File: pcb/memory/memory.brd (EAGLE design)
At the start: 50 x 80 mm, 9 parts, among them IC1 CY62256LL-PXC, IC2 CY62256LL-PXC, IC3 74HC04D

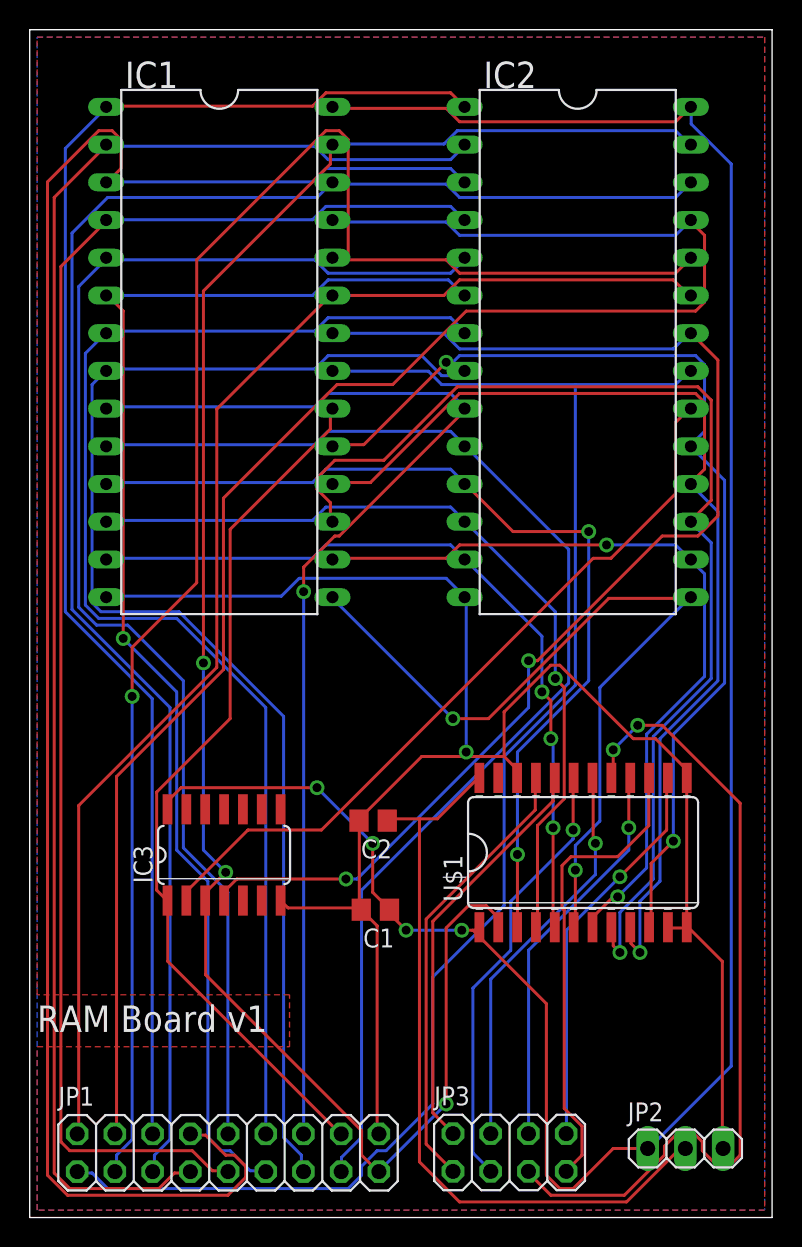
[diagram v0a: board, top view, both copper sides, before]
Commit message: Fixed pours and borders
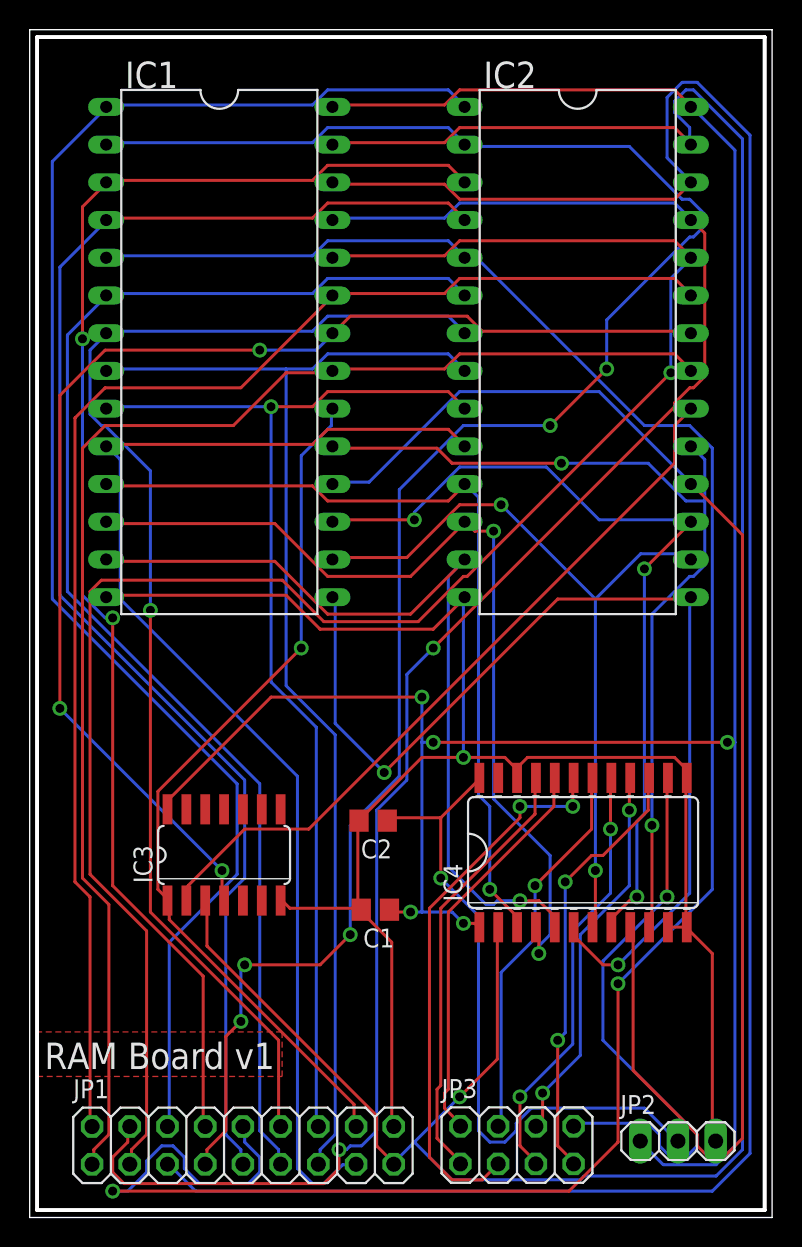
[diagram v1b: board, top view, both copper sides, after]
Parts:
- moved JP1 1.12 mm to (14.4, 4.86)
- moved JP2 0.71 mm to (43.7, 5.15)
- moved JP3 0.71 mm to (32.8, 4.88)
- renumbered U$1 to IC4
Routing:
- net A9: track 90.2 -> 148.9 mm, vias 0 -> 2
- net !WE!: track 127.1 -> 168.7 mm, vias 3 -> 1
- net A4: track 110.4 -> 148.5 mm
- net A7: track 121.5 -> 93.0 mm, vias 0 -> 2
- net D4: track 55.9 -> 29.0 mm
- net B6: track 70.2 -> 95.3 mm, vias 1 -> 0
- net A6: track 105.8 -> 127.6 mm, vias 0 -> 5
- net B5: track 75.7 -> 57.3 mm, vias 1 -> 3
- net B3: track 56.5 -> 70.0 mm
- net +5V: track 153.6 -> 166.6 mm, vias 4 -> 5
- net D7: track 26.8 -> 39.3 mm
- net A0: track 104.5 -> 93.5 mm
- net A2: track 110.9 -> 121.5 mm
- net A12: track 88.6 -> 80.5 mm
- net B7: track 69.2 -> 61.2 mm
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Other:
- outline, holes or cut-outs redrawn

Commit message: More minor changes
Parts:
- renumbered IC4 to U$1
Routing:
- added copper zone on layer 16, net N$2
- added copper zone on layer 1, net N$3
- removed copper zone on layer 1, net N$2
- removed copper zone on layer 16, net N$3
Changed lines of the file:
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@@
 <layers>
 <layer number="1" name="Top" color="4" fill="1" visible="yes" active="yes"/>
-<layer number="16" name="Bottom" color="1" fill="1" visible="yes" active="yes"/>
+<layer number="16" name="Bottom" color="1" fill="1" visible="no" active="yes"/>
 <layer number="17" name="Pads" color="2" fill="1" visible="yes" active="yes"/>
 <layer number="18" name="Vias" color="2" fill="1" visible="yes" active="yes"/>
@@
 <element name="JP2" library="pinhead" package="1X03" value="PWR" x="43.66" y="5.15"/>
 <element name="JP3" library="pinhead" package="2X04" value="" x="32.82" y="4.88"/>
-<element name="IC4" library="depmod" package="SO24W" value="74LCC4245A" x="37.27" y="24.58"/>
+<element name="U$1" library="depmod" package="SO24W" value="74LCC4245A" x="37.27" y="24.58"/>
 </elements>
 <signals>
 <signal name="D7">
-<contactref element="IC4" pad="14"/>
+<contactref element="U$1" pad="14"/>
 <contactref element="JP3" pad="8"/>
 <wire x1="42.926" y1="21.59" x2="42.926" y2="29.464" width="0.2032" layer="1"/>
@@
 </signal>
 <signal name="D6">
-<contactref element="IC4" pad="15"/>
+<contactref element="U$1" pad="15"/>
 <contactref element="JP3" pad="7"/>
 <wire x1="41.656" y1="27.432" x2="41.656" y2="29.464" width="0.2032" layer="1"/>
@@
 </signal>
 <signal name="D5">
-<contactref element="IC4" pad="16"/>
+<contactref element="U$1" pad="16"/>
 <contactref element="JP3" pad="6"/>
 <wire x1="40.386" y1="27.432" x2="40.386" y2="29.464" width="0.2032" layer="1"/>
@@
 </signal>
 <signal name="D4">
-<contactref element="IC4" pad="17"/>
+<contactref element="U$1" pad="17"/>
 <contactref element="JP3" pad="5"/>
 <wire x1="39.116" y1="26.162" x2="39.116" y2="29.464" width="0.2032" layer="1"/>
@@
 </signal>
 <signal name="D3">
-<contactref element="IC4" pad="18"/>
+<contactref element="U$1" pad="18"/>
 <contactref element="JP3" pad="4"/>
 <wire x1="37.846" y1="26.162" x2="37.846" y2="29.464" width="0.2032" layer="1"/>
@@
 </signal>
 <signal name="D2">
-<contactref element="IC4" pad="19"/>
+<contactref element="U$1" pad="19"/>
 <contactref element="JP3" pad="3"/>
 <wire x1="36.576" y1="27.686" x2="36.576" y2="29.464" width="0.2032" layer="1"/>
@@
 </signal>
 <signal name="D1">
-<contactref element="IC4" pad="20"/>
+<contactref element="U$1" pad="20"/>
 <contactref element="JP3" pad="2"/>
 <wire x1="35.306" y1="27.686" x2="35.306" y2="29.464" width="0.2032" layer="1"/>
@@
 </signal>
 <signal name="D0">
-<contactref element="IC4" pad="21"/>
+<contactref element="U$1" pad="21"/>
 <contactref element="JP3" pad="1"/>
 <wire x1="34.036" y1="27.178" x2="34.036" y2="29.464" width="0.2032" layer="1"/>
@@
 </signal>
 <signal name="+3V3">
-<contactref element="IC4" pad="24"/>
+<contactref element="U$1" pad="24"/>
 <contactref element="C2" pad="1"/>
 <contactref element="JP2" pad="2"/>
@@
 </signal>
 <signal name="GND">
-<contactref element="IC4" pad="12"/>
-<contactref element="IC4" pad="11"/>
-<contactref element="IC4" pad="13"/>
-<contactref element="IC4" pad="22"/>
+<contactref element="U$1" pad="12"/>
+<contactref element="U$1" pad="11"/>
+<contactref element="U$1" pad="13"/>
+<contactref element="U$1" pad="22"/>
 <contactref element="C1" pad="2"/>
 <contactref element="C2" pad="2"/>
@@
 <contactref element="IC2" pad="27"/>
 <contactref element="IC3" pad="3"/>
-<contactref element="IC4" pad="2"/>
+<contactref element="U$1" pad="2"/>
 <contactref element="JP1" pad="17"/>
 <wire x1="27.94" y1="72.39" x2="20.574" y2="72.39" width="0.2032" layer="1"/>
@@
 <contactref element="IC1" pad="11"/>
 <contactref element="IC2" pad="11"/>
-<contactref element="IC4" pad="3"/>
+<contactref element="U$1" pad="3"/>
 <wire x1="32.766" y1="20.32" x2="32.766" y2="19.558" width="0.2032" layer="1"/>
 <wire x1="30.988" y1="22.098" x2="32.766" y2="20.32" width="0.2032" layer="1"/>
@@
 <contactref element="IC1" pad="12"/>
 <contactref element="IC2" pad="12"/>
-<contactref element="IC4" pad="4"/>
+<contactref element="U$1" pad="4"/>
 <wire x1="34.29" y1="17.78" x2="34.29" y2="19.304" width="0.2032" layer="1"/>
 <wire x1="34.29" y1="18.288" x2="34.29" y2="17.78" width="0.2032" layer="16"/>
@@
 <contactref element="IC1" pad="13"/>
 <contactref element="IC2" pad="13"/>
-<contactref element="IC4" pad="5"/>
+<contactref element="U$1" pad="5"/>
 <wire x1="35.306" y1="20.32" x2="35.306" y2="19.558" width="0.2032" layer="1"/>
 <wire x1="34.29" y1="21.336" x2="35.306" y2="20.32" width="0.2032" layer="1"/>
@@
 <contactref element="IC1" pad="15"/>
 <contactref element="IC2" pad="15"/>
-<contactref element="IC4" pad="6"/>
+<contactref element="U$1" pad="6"/>
 <wire x1="36.83" y1="18.796" x2="36.83" y2="19.304" width="0.2032" layer="1"/>
 <wire x1="38.608" y1="17.018" x2="36.83" y2="18.796" width="0.2032" layer="1"/>
@@
 <contactref element="IC1" pad="16"/>
 <contactref element="IC2" pad="16"/>
-<contactref element="IC4" pad="7"/>
+<contactref element="U$1" pad="7"/>
 <wire x1="38.1" y1="23.368" x2="38.1" y2="19.558" width="0.2032" layer="1"/>
 <wire x1="38.1" y1="41.656" x2="38.1" y2="23.368" width="0.2032" layer="16"/>
@@
 <contactref element="IC1" pad="17"/>
 <contactref element="IC2" pad="17"/>
-<contactref element="IC4" pad="8"/>
+<contactref element="U$1" pad="8"/>
 <wire x1="39.37" y1="20.32" x2="39.37" y2="19.558" width="0.2032" layer="1"/>
 <wire x1="40.64" y1="21.59" x2="39.37" y2="20.32" width="0.2032" layer="1"/>
@@
 <contactref element="IC1" pad="18"/>
 <contactref element="IC2" pad="18"/>
-<contactref element="IC4" pad="9"/>
+<contactref element="U$1" pad="9"/>
 <wire x1="40.64" y1="9.906" x2="40.64" y2="19.304" width="0.2032" layer="1"/>
 <wire x1="44.958" y1="5.588" x2="40.64" y2="9.906" width="0.2032" layer="1"/>
@@
 <contactref element="IC1" pad="19"/>
 <contactref element="IC2" pad="19"/>
-<contactref element="IC4" pad="10"/>
+<contactref element="U$1" pad="10"/>
 <wire x1="41.91" y1="26.416" x2="41.91" y2="19.558" width="0.2032" layer="1"/>
 <wire x1="41.91" y1="40.64" x2="41.91" y2="26.416" width="0.2032" layer="16"/>
@@
 <contactref element="IC1" pad="28"/>
 <contactref element="IC2" pad="28"/>
-<contactref element="IC4" pad="1"/>
+<contactref element="U$1" pad="1"/>
 <contactref element="JP2" pad="1"/>
 <contactref element="C1" pad="1"/>
@@
 </signal>
 <signal name="N$2">
+<polygon width="0.254" layer="16">
+<vertex x="0.5" y="79.5"/>
+<vertex x="49.5" y="79.5"/>
+<vertex x="49.5" y="0.5"/>
+<vertex x="0.5" y="0.5"/>
+</polygon>
+</signal>
+<signal name="N$3">
 <polygon width="0.254" layer="1">
 <vertex x="0.5" y="9.5"/>
-<vertex x="17" y="9.5"/>
-<vertex x="17" y="12.5"/>
+<vertex x="17.5" y="9.5"/>
+<vertex x="17.5" y="12.5"/>
 <vertex x="0.5" y="12.5"/>
 <vertex x="0.5" y="79.5"/>
 <vertex x="49.5" y="79.5"/>
-<vertex x="49.5" y="79"/>
-<vertex x="49.5" y="0.5"/>
-<vertex x="0.5" y="0.5"/>
-</polygon>
-</signal>
-<signal name="N$3">
-<polygon width="0.254" layer="16">
-<vertex x="0.5" y="79.5"/>
-<vertex x="49.5" y="79.5"/>
